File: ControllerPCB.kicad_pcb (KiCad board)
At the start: 2 copper layers, 23 parts, among them J1 Conn_01x02_Male, J10 Conn_01x06_Male, J2 Conn_01x04_Male, J3 Conn_01x02_Male, J4 Conn_01x02_Male, J5 Conn_01x03_Male, J6 Conn_01x02_Male, J7 A-2004-2-4-LPS-N-R, J8 Conn_01x04_Male, J9 Conn_01x04_Male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

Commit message: V2
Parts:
- added D4: D, Diode_THT:D_DO-15_P15.24mm_Horizontal, F.Cu at (125.0, 97.3)
- added J11: Conn_01x02_Male, Connector_PinHeader_2.54mm:PinHeader_1x02_P2.54mm_Vertical, F.Cu at (175.0, 60.0)
- added J12: Conn_01x02_Male, Connector_PinHeader_2.54mm:PinHeader_1x02_P2.54mm_Vertical, F.Cu at (175.0, 75.0)
- D1, D2, D3: value DIODE -> D; footprint Diode_THT:D_5KP_P12.70mm_Horizontal -> Diode_THT:D_DO-15_P15.24mm_Horizontal
- J4: value Conn_01x02_Male -> Conn_01x03_Male; footprint Connector_PinHeader_2.54mm:PinHeader_1x02_P2.54mm_Vertical -> Connector_PinHeader_2.54mm:PinHeader_1x03_P2.54mm_Vertical
- moved J9 155.5 mm to (235.0, 69.0)
- moved J4 132.2 mm to (235.0, 45.0)
- moved Q2 103.6 mm to (175.0, 134.0), turned to 90 degrees
- moved R4 100.4 mm to (160.0, 89.5)
- moved R3 99.2 mm to (160.0, 99.5)
- moved J10 97.7 mm to (205.0, 64.0)
- moved J8 94.6 mm to (220.0, 69.0)
- moved J2 94.4 mm to (190.0, 69.0)
- moved J6 83.3 mm to (175.0, 44.0)
- moved Q1 81.7 mm to (155.0, 134.0), turned to 90 degrees
- moved U1 80.9 mm to (200.0, 129.0)
- moved J5 80.6 mm to (220.0, 44.0)
- moved J7 80.2 mm to (132.5, 48.5)
- moved P1 80.2 mm to (157.0, 47.0)
- moved XA1 80.2 mm to (56.5, 41.5)
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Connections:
- D1 pad 1: Fans- -> Net-(D1-Pad1)
- D1 pad 2: Net-(D1-Pad2) -> Fans-
- D2 pad 1: RollerMotor- -> Net-(D2-Pad1)
- D2 pad 2: Net-(D2-Pad2) -> RollerMotor-
- D3 pad 1: RollerMotor- -> +5V
- D3 pad 2: Encoder+ -> RollerMotor-
- J1 pad 1: ScrewMotor -> GND
- J1 pad 2: Encoder- -> ScrewMotor
- J10 pad 1: Encoder+ -> +5V
- J10 pad 3: Encoder- -> GND
- J10 pad 4: Encoder+ -> +5V
- J2 pad 1: +3V3 -> GND
- J2 pad 2: Encoder- -> SlackS0
- J2 pad 3: SlackS0 -> SlackS1
- J2 pad 4: SlackS1 -> +5V
- J3 pad 1: SpollerMotor -> GND
- J3 pad 2: Encoder- -> SpollerMotor
- J4 pad 1: Encoder+ -> GND
- J4 pad 2: Encoder- -> +5V
- J5 pad 1: +3V3 -> GND
- J5 pad 3: Encoder- -> +5V
- J6 pad 1: Encoder+ -> Fans-
- J6 pad 2: Fans- -> +5V
- J7 pad 1: Encoder+ -> +5V
- J7 pad 4: Encoder- -> GND
- J7 pad S1: Encoder- -> GND
- J7 pad S2: Encoder- -> GND
- J8 pad 1: Encoder- -> GND
- J8 pad 4: Encoder+ -> +5V
- J9 pad 1: Encoder- -> GND
- J9 pad 4: Encoder+ -> +5V
- P1 pad 3: Net-(P1-Pad3) -> LV2
- P1 pad 4: Encoder- -> GND
- Q1 pad 2: Encoder- -> GND
- Q1 pad 3: Net-(D1-Pad2) -> Net-(D1-Pad1)
- Q2 pad 2: Encoder- -> GND
- Q2 pad 3: Net-(D2-Pad2) -> Net-(D2-Pad1)
- R1 pad 1: +3V3 -> +5V
- R2 pad 1: +3V3 -> +5V
- R3 pad 2: Encoder- -> GND
- R4 pad 2: Encoder- -> GND
- U1 pad GND_1: Encoder- -> GND
- U1 pad GND_2: Encoder- -> GND
- U1 pad HV: Encoder+ -> +5V
- U1 pad HV1: DialData -> DialCLK
- U1 pad HV2: DialCLK -> DialData
- U1 pad LV1: Net-(P1-Pad3) -> Net-(P1-Pad2)
- U1 pad LV2: Net-(P1-Pad2) -> LV2
- XA1 pad 5V1: Encoder+ -> Net-(XA1-Pad5V1)
- XA1 pad 5V3: Encoder+ -> Net-(XA1-Pad5V3)
- XA1 pad 5V4: Encoder+ -> Net-(XA1-Pad5V4)
- XA1 pad D10: ScaleD1 -> Net-(XA1-PadD10)
- XA1 pad D11: ScaleD2 -> Net-(XA1-PadD11)
- XA1 pad D12: ScaleCLK1 -> Net-(XA1-PadD12)
- XA1 pad D13: ScaleCLK2 -> Net-(XA1-PadD13)
- XA1 pad GND1: Encoder- -> GND
- XA1 pad GND2: Encoder- -> GND
- XA1 pad GND3: Encoder- -> GND
- XA1 pad GND5: Encoder- -> GND
- XA1 pad GND6: Encoder- -> GND
- XA2 pad 3V3: +3V3 -> Net-(XA2-Pad3V3)
- XA2 pad 5V: Encoder+ -> Net-(XA2-Pad5V)
- XA2 pad D1: TX0 -> TX1
- XA2 pad D4: Net-(XA2-PadD4) -> ScaleCLK1
- XA2 pad D5: Net-(XA2-PadD5) -> ScaleD2
- XA2 pad D6: Net-(XA2-PadD6) -> ScaleD1
- XA2 pad D7: Net-(XA2-PadD7) -> ScaleCLK2
- XA2 pad GND1: Encoder- -> GND
- XA2 pad GND2: Encoder- -> GND
- XA2 pad VIN: Net-(XA2-PadVIN) -> Vin
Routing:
- net +5V: track 0.00 -> 406.9 mm, vias 0 -> 4
- net Vin: track 0.00 -> 291.8 mm, vias 0 -> 1
- net TactSignal: track 0.00 -> 199.4 mm, vias 0 -> 1
- net ScrewMotor: track 0.00 -> 174.3 mm, vias 0 -> 1
- net SpollerMotor: track 0.00 -> 150.8 mm, vias 0 -> 1
- net TX1: track 0.00 -> 145.2 mm, vias 0 -> 1
- net RX1: track 0.00 -> 141.8 mm, vias 0 -> 1
- net EncoderA: track 0.00 -> 121.7 mm, vias 0 -> 1
- net EncoderB: track 0.00 -> 117.2 mm, vias 0 -> 1
- net RollerMotor-: track 0.00 -> 110.7 mm, vias 0 -> 1
- net SCL: track 0.00 -> 107.9 mm, vias 0 -> 1
- net LV2: track 0.00 -> 104.8 mm, vias 0 -> 2
- net Net-(P1-Pad1): track 0.00 -> 103.9 mm, vias 0 -> 2
- net Net-(P1-Pad2): track 0.00 -> 101.6 mm, vias 0 -> 2
- net SDA: track 0.00 -> 99.2 mm, vias 0 -> 1
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- added copper zone on B.Cu, net GND
- added copper zone on F.Cu, net GND
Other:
- board outline added: 220 x 125 mm
- board text added: "10k"
- board text added: "Fan"
- board text added: "GND 5V Vin"
- board text added: "Gate"
- board text added: "Power"
- board text added: "Rollers"
- board text added: "SCL"
- board text added: "SDA"
- board text added: "Scale"
- board text added: "Screw"
- board text added: "Slack Sensor"
- board text added: "Spoller"
- board text added: "Tachometer"

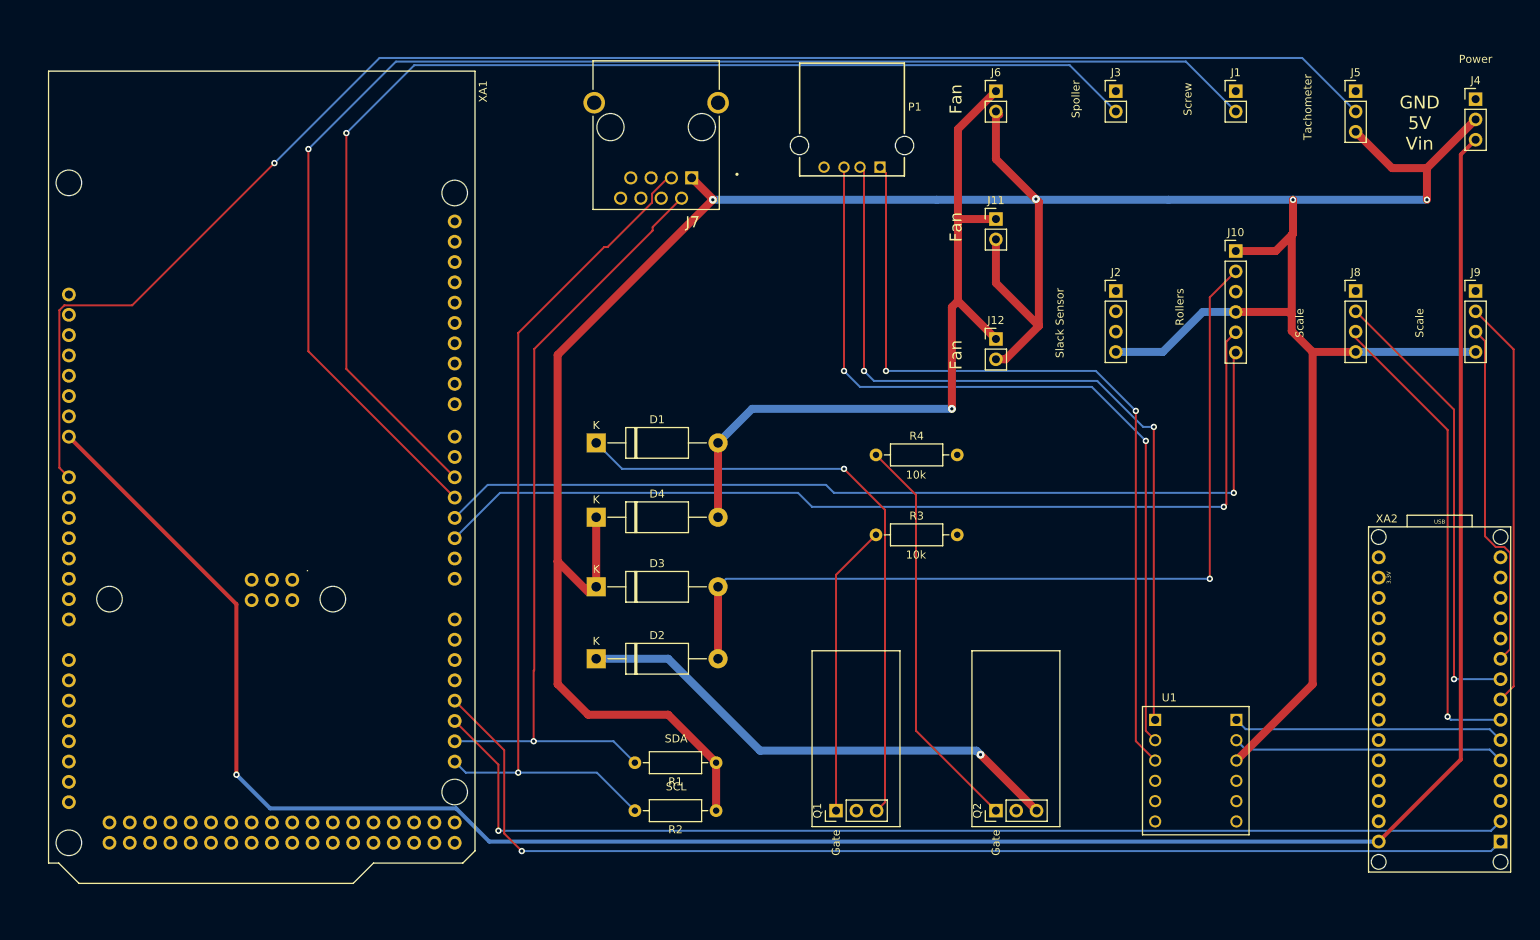
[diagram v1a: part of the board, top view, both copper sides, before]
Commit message: Flipped Arduino
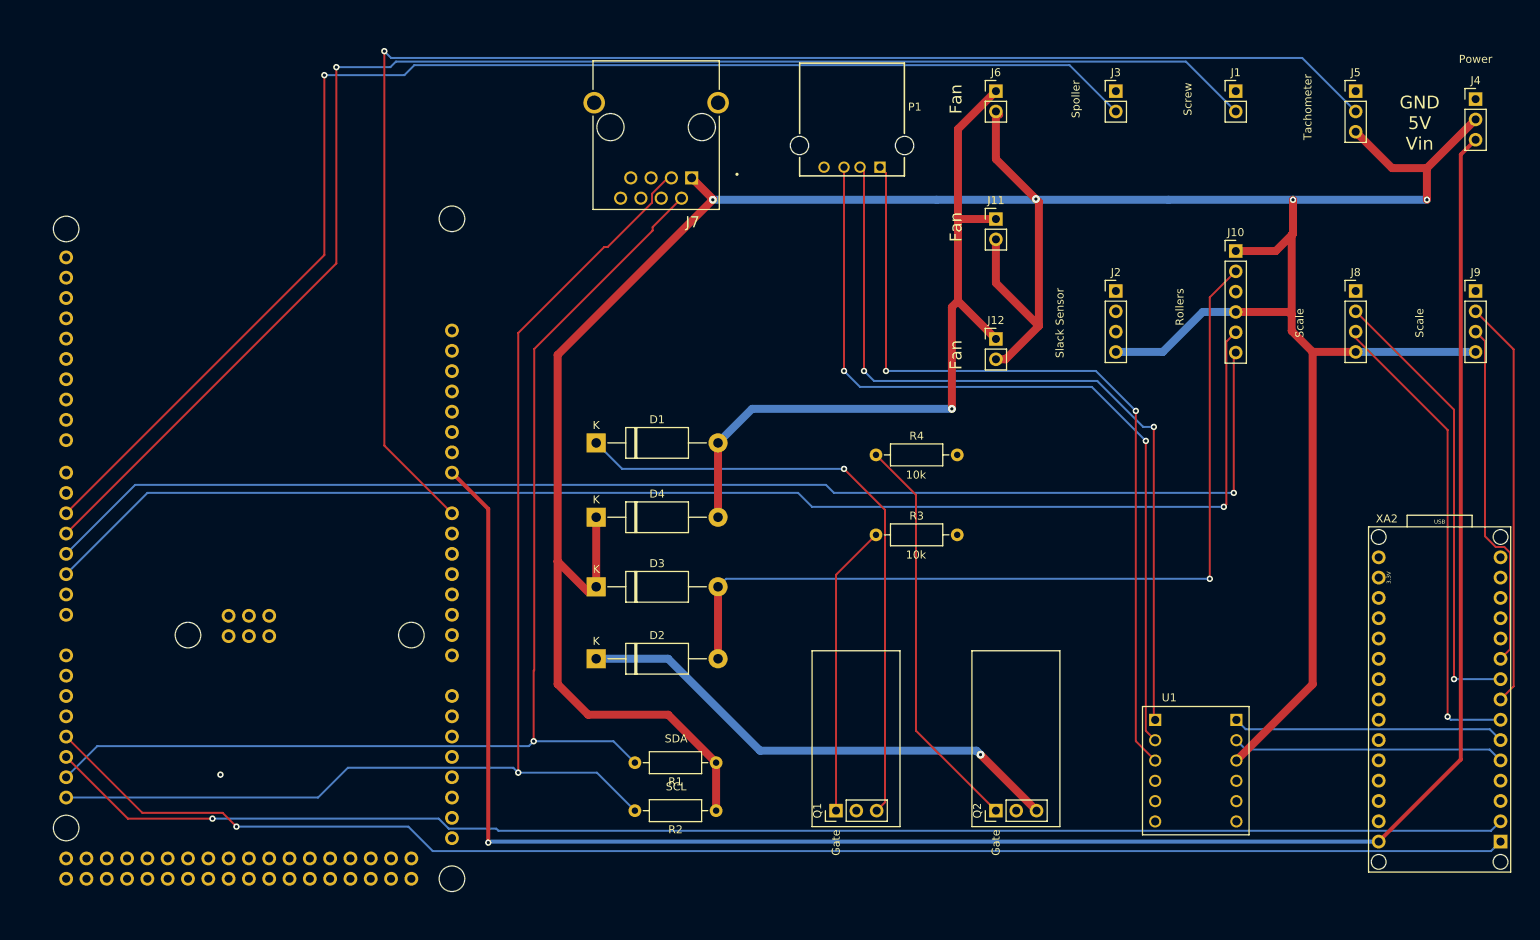
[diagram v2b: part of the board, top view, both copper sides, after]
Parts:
- XA1: moved to B.Cu
- moved XA1 53.2 mm to (109.5, 46.0)
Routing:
- net SDA: track 99.2 -> 149.7 mm
- net EncoderB: track 117.2 -> 167.7 mm
- net EncoderA: track 121.7 -> 172.2 mm
- net SCL: track 107.9 -> 157.7 mm
- net RX1: track 141.8 -> 183.7 mm
- net TX1: track 145.2 -> 185.8 mm
- net Vin: track 291.8 -> 253.9 mm
- net SpollerMotor: track 150.8 -> 170.1 mm
- net TactSignal: track 199.4 -> 185.9 mm
- net ScrewMotor: track 174.3 -> 187.7 mm
- net GND: vias 4 -> 5

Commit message: Add plot files
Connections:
- XA1 pad D14: Net-(XA1-PadD14) -> UartToNano
- XA1 pad D15: Net-(XA1-PadD15) -> UartToMega
- XA1 pad D18: TX1 -> Net-(XA1-PadD18)
- XA1 pad D19: RX1 -> Net-(XA1-PadD19)
- XA2 pad D0: RX1 -> UartToNano
- XA2 pad D1: TX1 -> UartToMega
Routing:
- net UartToMega: track 0.00 -> 190.5 mm, vias 0 -> 1
- net UartToNano: track 0.00 -> 190.2 mm, vias 0 -> 1
- net TX1: track 185.8 -> 0.00 mm, vias 1 -> 0
- net RX1: track 183.7 -> 0.00 mm, vias 1 -> 0
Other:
- board text added: "Created by Team 09 of Valpo Engineering Design Team"

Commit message: Fixed two unconnected pads
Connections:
- Q2 pad 1: RollerMotor -> RollerSpeed
- R4 pad 1: RollerMotor -> RollerSpeed
- XA1 pad A1: Net-(XA1-PadA1) -> SlackS0
- XA1 pad A2: Net-(XA1-PadA2) -> SlackS1
- XA1 pad D6: Net-(XA1-PadD6) -> FansSpeed
- XA1 pad D7: Net-(XA1-PadD7) -> RollerSpeed
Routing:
- net RollerSpeed: track 0.00 -> 158.3 mm
- net SlackS1: track 0.00 -> 134.2 mm, vias 0 -> 1
- net SlackS0: track 0.00 -> 128.5 mm, vias 0 -> 1
- net FansSpeed: track 36.6 -> 155.8 mm, vias 0 -> 1
- net RollerMotor: track 50.7 -> 0.00 mm
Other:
- board text added: "Scale1"
- board text added: "Scale2"
- board text removed: "Scale"

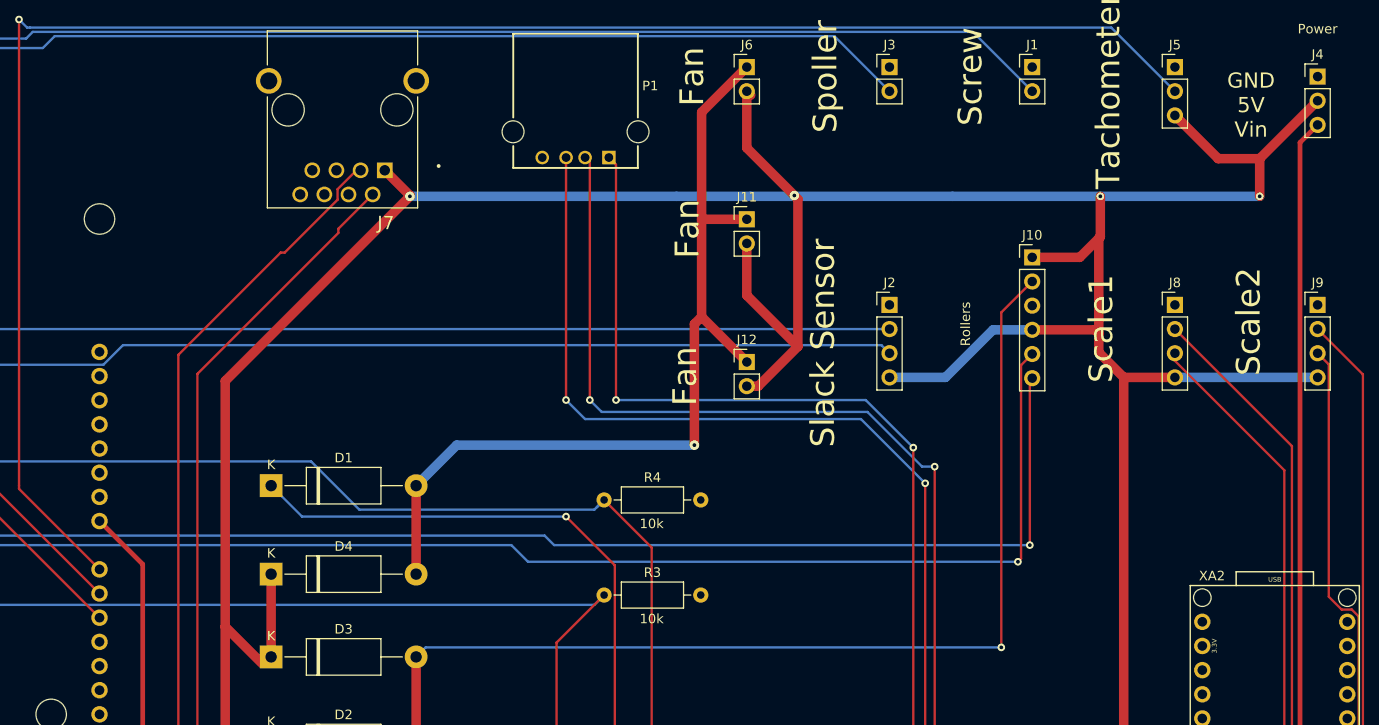
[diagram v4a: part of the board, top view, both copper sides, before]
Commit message: Updated 5V and 5Vin
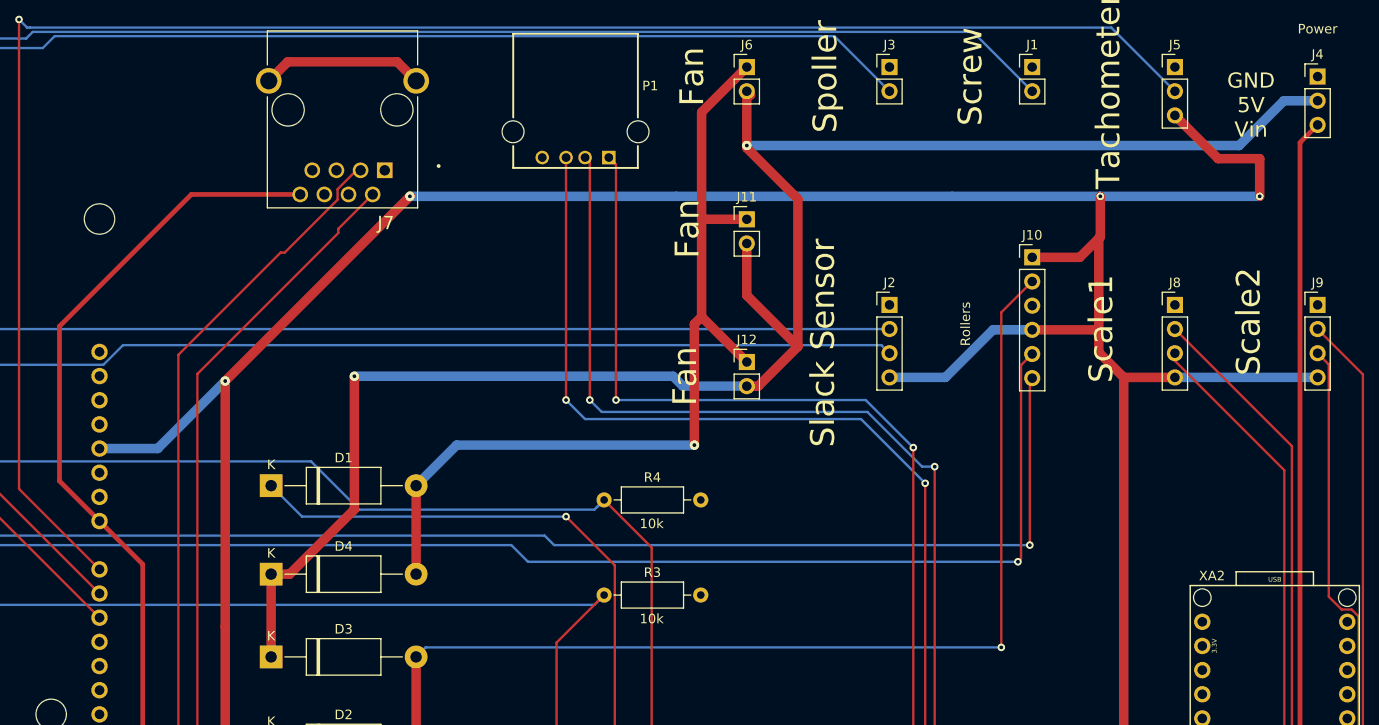
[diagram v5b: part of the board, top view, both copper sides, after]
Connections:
- D3 pad 1: +5V -> 5Vin
- D4 pad 1: +5V -> 5Vin
- J11 pad 2: +5V -> 5Vin
- J12 pad 2: +5V -> 5Vin
- J4 pad 2: +5V -> 5Vin
- J6 pad 2: +5V -> 5Vin
- J7 pad 1: +5V -> Net-(J7-Pad1)
- J7 pad 8: Net-(J7-Pad8) -> Vin
- XA1 pad 5V1: Net-(XA1-Pad5V1) -> +5V
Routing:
- net 5Vin: track 0.00 -> 187.7 mm, vias 0 -> 2
- net +5V: track 406.9 -> 346.7 mm
- net Vin: track 253.9 -> 307.1 mm
- net GND: track 0.00 -> 17.2 mm
